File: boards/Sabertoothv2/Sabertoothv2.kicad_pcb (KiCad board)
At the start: 2 copper layers, 39 parts, among them J1 Screw_Terminal_01x04, J2 Screw_Terminal_01x04, J4 Conn_01x04_Pin, J5 Conn_01x04_Pin, Q1 NMOS, Q2 NMOS, Q3 NMOS, Q4 NMOS, U1 LM2104, U2 LM2104, U4 74LVC1GU04DRL

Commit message: PCB update
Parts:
- J2: footprint TerminalBlock:TerminalBlock_bornier-4_P5.08mm -> TerminalBlock_TE-Connectivity:TerminalBlock_TE_282834-4_1x04_P2.54mm_Horizontal
- Q1, Q2, Q3, Q4: footprint mosfet:TRANS_SI7232DN-T1-GE3 -> Package_SO:PowerPAK_SO-8_Single
- U1, U2: footprint Package_SO:SOIC-16_3.9x9.9mm_P1.27mm -> Package_SO:SOIC-8-1EP_3.9x4.9mm_P1.27mm_EP2.29x3mm
- moved D2 98.7 mm to (94.6, 101.9)
- moved D3 98.7 mm to (94.6, 104.9)
- moved D4 98.7 mm to (94.6, 108.0)
- moved D5 98.7 mm to (94.6, 111.0)
- moved D6 98.7 mm to (94.6, 114.0)
- moved DBOOT2 98.7 mm to (94.6, 120.1)
- moved D1 89.8 mm to (83.7, 96.8)
- moved U2 74.0 mm to (87.8, 107.6)
- moved CBOOT1 47.9 mm to (85.3, 68.4)
- moved CGVDD2 47.9 mm to (85.3, 77.4)
- moved Q2 47.9 mm to (93.7, 81.1)
- moved Q4 47.9 mm to (93.7, 90.8)
- moved R1 47.9 mm to (80.5, 80.4)
- moved R2 47.9 mm to (80.5, 83.4)
- moved R3 47.9 mm to (80.5, 86.3)
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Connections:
- CBOOT1 pad 2: LOAD -> LOAD1
- CBOOT2 pad 2: LOAD -> LOAD2
- Q1 pad 3: LOAD -> LOAD1
- Q2 pad 1: LOAD -> LOAD1
- Q3 pad 3: LOAD -> LOAD2
- Q4 pad 1: LOAD -> LOAD2
- U1 pad 6: LOAD -> LOAD1
- U2 pad 6: LOAD -> LOAD2
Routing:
- net OUT: track 0.00 -> 41.9 mm
- net VIN: track 0.00 -> 18.8 mm
- net Net-(U1-IN): track 0.00 -> 10.0 mm
- net Net-(DBOOT1-K): track 0.00 -> 7.57 mm
- net Net-(DBOOT1-A): track 0.00 -> 7.19 mm
- net GND: track 0.00 -> 1.25 mm

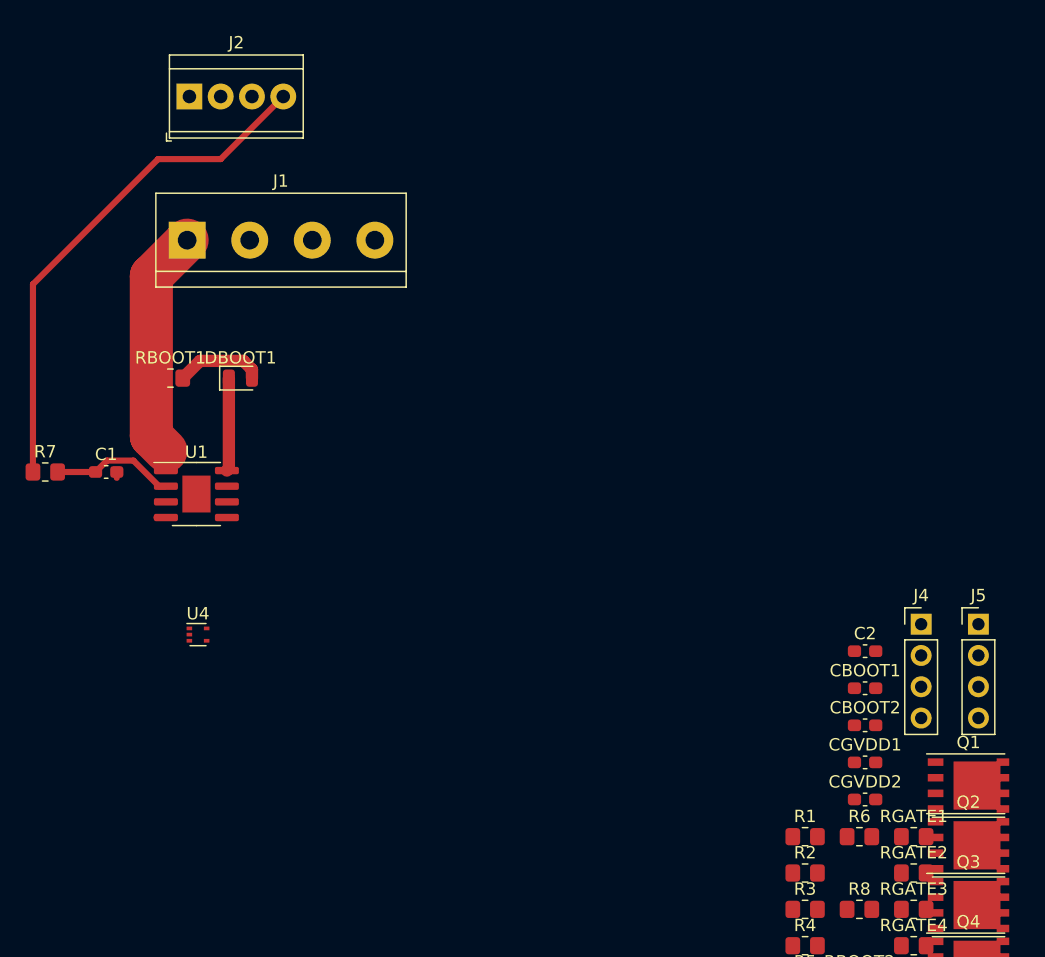
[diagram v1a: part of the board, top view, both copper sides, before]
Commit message: wired first driver
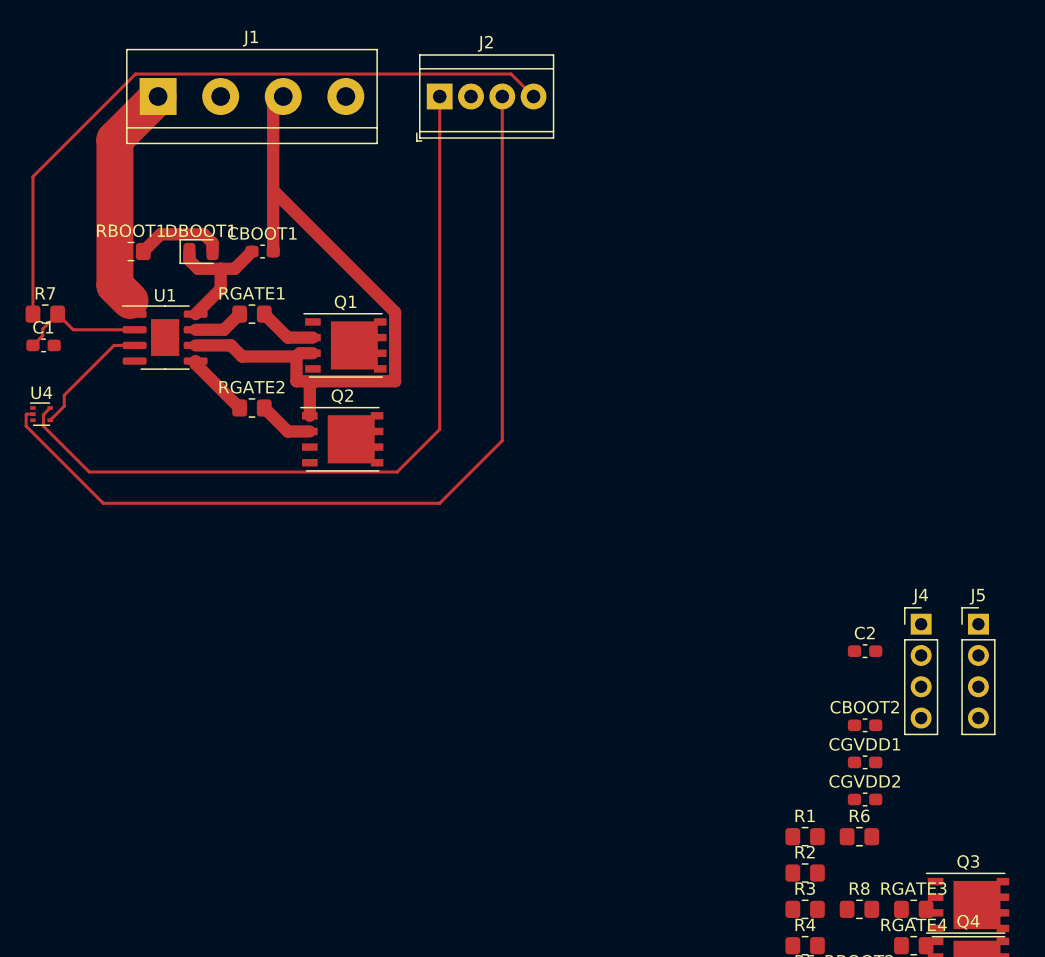
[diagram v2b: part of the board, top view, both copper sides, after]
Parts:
- moved RGATE1 68.5 mm to (35.6, 38.0)
- moved RGATE2 65.7 mm to (35.6, 45.6)
- moved Q1 61.9 mm to (43.2, 40.5)
- moved Q2 60.6 mm to (42.9, 48.1)
- moved CBOOT1 60.4 mm to (36.4, 32.9)
- moved U4 21.9 mm to (18.5, 46.1)
- moved J2 20.3 mm to (50.8, 20.3)
- moved U1 13.0 mm to (28.5, 39.9)
- moved R7 12.8 mm to (18.8, 38.0)
- moved J1 11.9 mm to (27.9, 20.3)
- moved C1 11.5 mm to (18.6, 40.5)
- moved DBOOT1 10.8 mm to (31.4, 32.9)
- moved RBOOT1 10.8 mm to (25.7, 32.9)
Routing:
- net SELECT: track 0.00 -> 72.8 mm
- net VCC+5: track 0.00 -> 63.9 mm
- net LOAD1: track 0.00 -> 55.5 mm
- net OUT: track 41.9 -> 56.0 mm
- net Net-(U1-SD'): track 0.00 -> 9.90 mm
- net Net-(U1-GL): track 0.00 -> 5.29 mm
- net HOA: track 0.00 -> 4.74 mm
- net LOA: track 0.00 -> 4.48 mm
- net Net-(U1-GH): track 0.00 -> 4.10 mm
- net Net-(DBOOT1-K): track 7.57 -> 11.2 mm
- net GND: track 1.25 -> 0.00 mm

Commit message: did some more stuff
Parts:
- moved DBOOT2 87.8 mm to (40.6, 50.8)
- moved U2 71.3 mm to (35.5, 59.2)
- moved CGVDD1 67.6 mm to (33.9, 30.5)
- moved J4 65.3 mm to (76.2, 127.0)
- moved RBOOT2 64.0 mm to (34.0, 53.3)
- moved R8 63.7 mm to (26.4, 61.0)
- moved C2 59.1 mm to (26.3, 63.5)
- moved CGVDD2 57.9 mm to (33.9, 50.8)
- moved RGATE3 56.1 mm to (42.2, 55.9)
- moved RGATE4 53.7 mm to (42.2, 63.5)
- moved Q3 51.0 mm to (50.8, 58.4)
- moved D5 50.8 mm to (109.2, 159.6)
- moved R4 50.8 mm to (95.2, 137.9)
- moved D1 50.8 mm to (98.4, 145.4)
- moved D2 50.8 mm to (109.2, 150.5)
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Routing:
- net VIN: track 18.5 -> 128.1 mm, vias 0 -> 2
- net LOAD2: track 0.00 -> 89.2 mm
- net Net-(DBOOT2-K): track 0.00 -> 14.9 mm
- net OUT: track 56.0 -> 69.3 mm, vias 0 -> 3
- net Net-(U2-IN): track 0.00 -> 9.99 mm
- net VCC+5: track 63.9 -> 54.3 mm, vias 0 -> 2
- net Net-(DBOOT2-A): track 0.00 -> 8.02 mm
- net HOB: track 0.00 -> 5.74 mm
- net LOB: track 0.00 -> 5.64 mm
- net Net-(U2-GH): track 0.00 -> 4.72 mm
- net LOAD1: track 55.5 -> 60.2 mm
- net Net-(U2-GL): track 0.00 -> 4.21 mm
- net Net-(U1-IN): track 10.1 -> 7.61 mm
- net Net-(DBOOT1-K): track 11.2 -> 13.3 mm
- net LOA: track 4.48 -> 6.60 mm
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
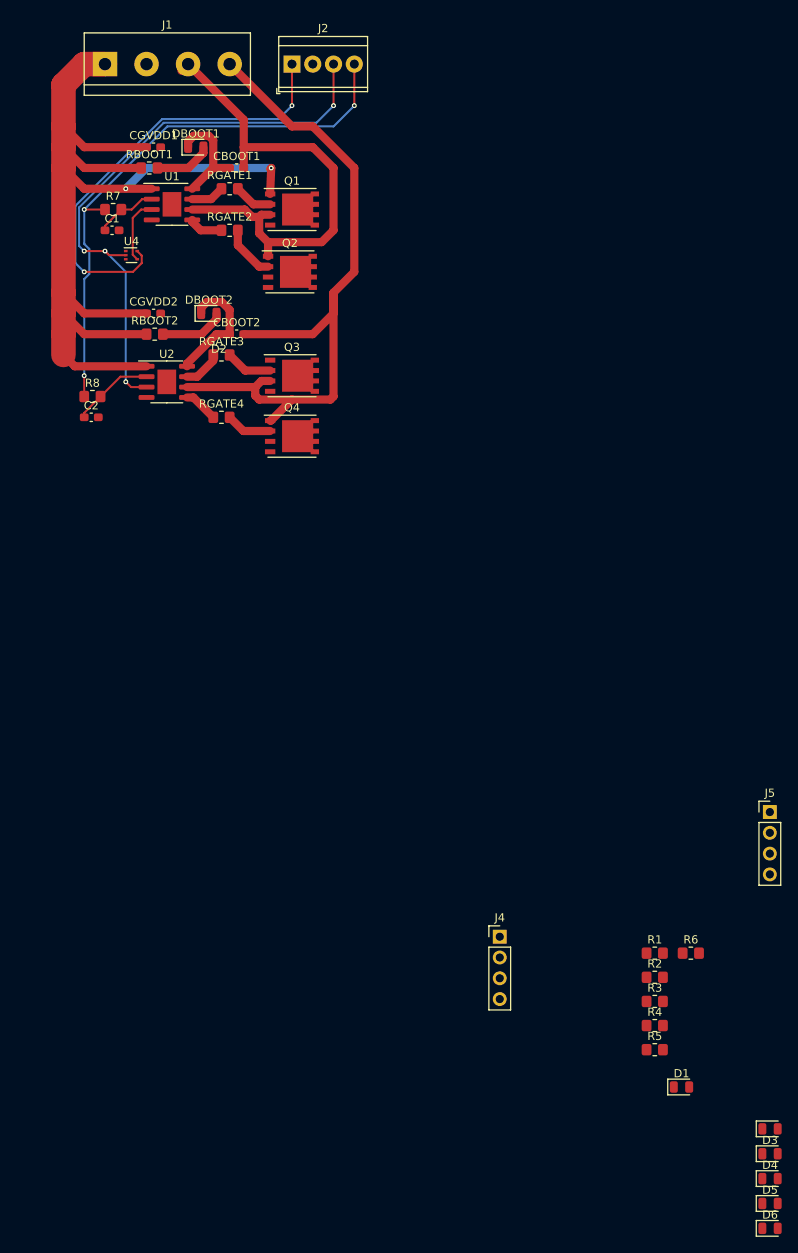
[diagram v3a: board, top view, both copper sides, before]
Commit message: Nathan's new version of the test board with edited silkscreen and logo
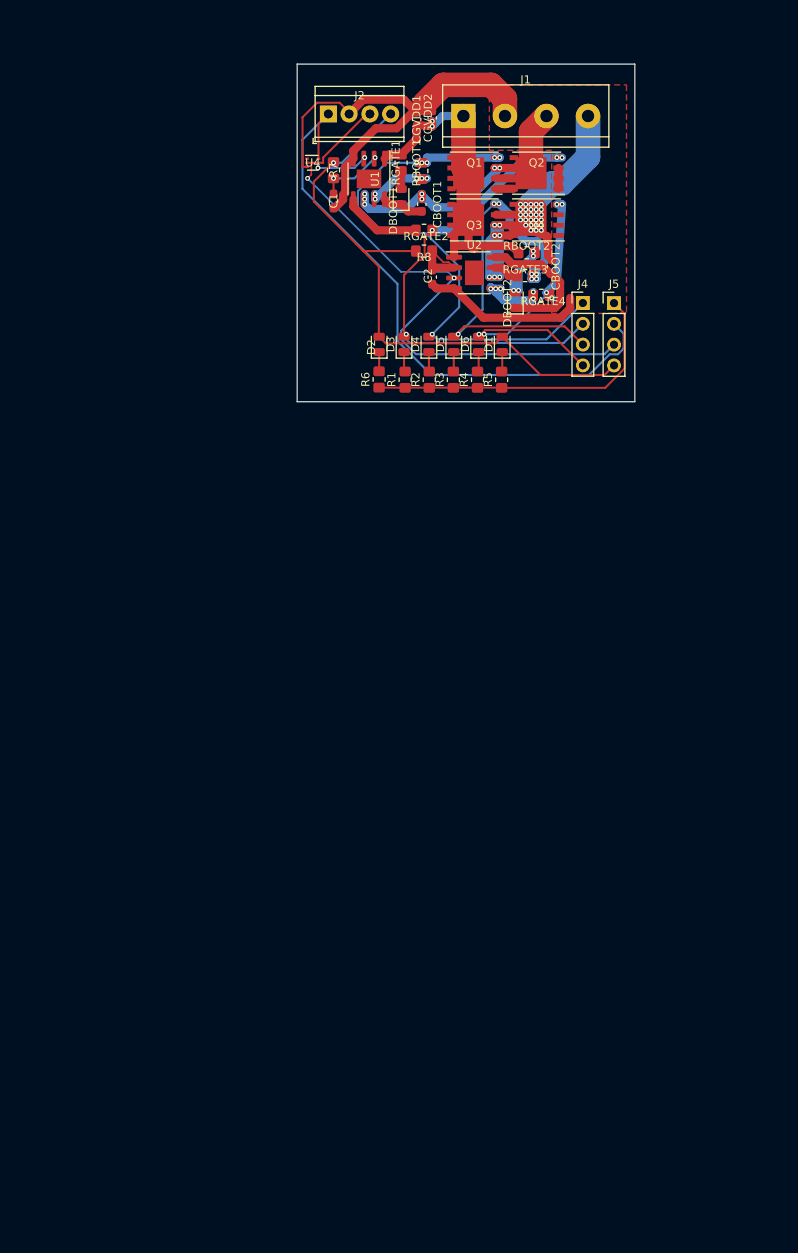
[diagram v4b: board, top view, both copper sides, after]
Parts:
- added G***: LOGO, LOGO, B.Cu at (71.1, 40.0)
- moved D6 113.8 mm to (73.6, 54.6), turned to 90 degrees
- moved D5 111.9 mm to (70.6, 54.6), turned to 90 degrees
- moved D4 110.2 mm to (67.5, 54.6), turned to 90 degrees
- moved D3 108.6 mm to (64.5, 54.6), turned to 90 degrees
- moved D2 107.1 mm to (61.5, 54.6), turned to 90 degrees
- moved D1 93.4 mm to (76.5, 54.6), turned to 90 degrees
- moved R5 84.0 mm to (76.4, 58.9), turned to 90 degrees
- moved R4 81.9 mm to (73.5, 58.9), turned to 90 degrees
- moved R3 79.9 mm to (70.5, 58.9), turned to 90 degrees
- moved R6 79.8 mm to (61.5, 58.9), turned to 90 degrees
- moved J4 78.1 mm to (86.4, 49.5)
- moved R2 78.1 mm to (67.6, 58.9), turned to 90 degrees
- moved R1 76.5 mm to (64.6, 58.9), turned to 90 degrees
- moved J5 65.1 mm to (90.2, 49.5)
- moved RBOOT2 46.6 mm to (79.5, 43.4)
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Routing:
- net GND: track 0.00 -> 119.9 mm
- net VIN: track 128.1 -> 44.5 mm
- net HOA: track 4.74 -> 68.1 mm, vias 0 -> 6
- net LOA: track 6.60 -> 57.8 mm, vias 0 -> 4
- net HOB: track 5.74 -> 50.9 mm, vias 0 -> 7
- net LOB: track 5.64 -> 38.3 mm, vias 0 -> 6
- net LOAD1: track 60.2 -> 37.4 mm, vias 0 -> 7
- net VCC+5: track 54.3 -> 74.1 mm, vias 2 -> 0
- net LOAD2: track 89.2 -> 78.1 mm, vias 0 -> 34
- net Net-(DBOOT1-K): track 13.3 -> 5.18 mm
- net Net-(U1-GL): track 4.24 -> 9.75 mm
- net OUT: track 69.3 -> 74.6 mm, vias 3 -> 1
- net Net-(DBOOT1-A): track 7.08 -> 2.21 mm
- net Net-(U2-GL): track 4.21 -> 8.58 mm, vias 0 -> 5
- net Net-(U1-GH): track 4.10 -> 8.04 mm, vias 0 -> 5
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- added copper zone on F.Cu, net GND
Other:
- board outline added: 41.3 x 41.3 mm
- board text added: "Nathan Colunga Lee Buffett Emily Lory Joseph Hanger"
